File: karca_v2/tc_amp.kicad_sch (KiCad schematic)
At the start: 16 parts, among them U17 TLV9304xD, U22 AD8495

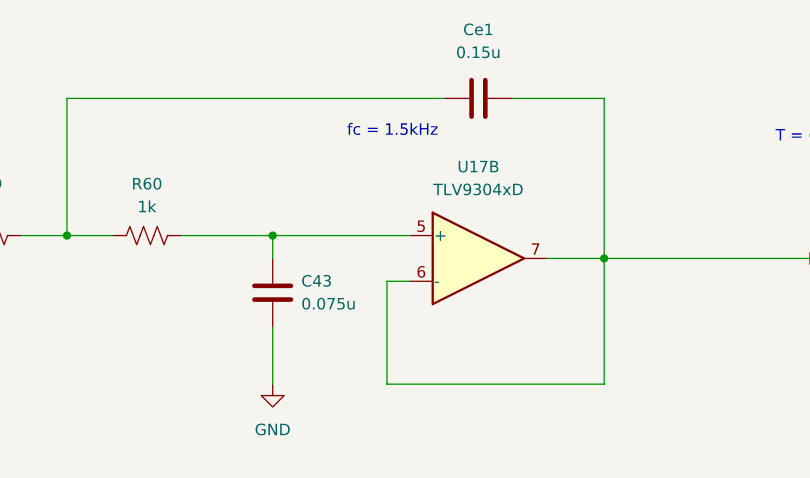
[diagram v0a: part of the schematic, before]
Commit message: changed capacitor values and sizes for production
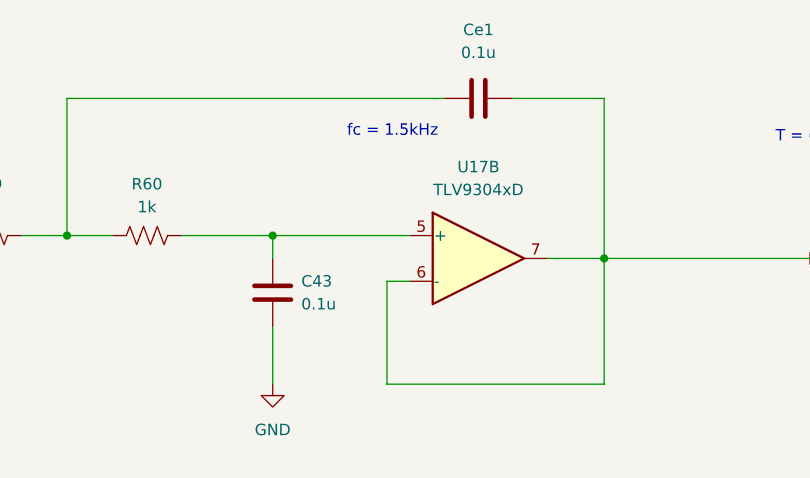
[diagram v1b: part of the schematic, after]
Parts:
- C43: value 0.075u -> 0.1u
- Ce1: value 0.15u -> 0.1u
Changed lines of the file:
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@@
       (effects (font (size 1.27 1.27)) (justify left))
     )
-    (property "Value" "0.075u" (at 196.85 62.23 0)
+    (property "Value" "0.1u" (at 196.85 62.23 0)
       (effects (font (size 1.27 1.27)) (justify left))
     )
@@
       (effects (font (size 1.27 1.27)))
     )
-    (property "Value" "0.15u" (at 216.535 34.29 90)
+    (property "Value" "0.1u" (at 216.535 34.29 90)
       (effects (font (size 1.27 1.27)))
     )

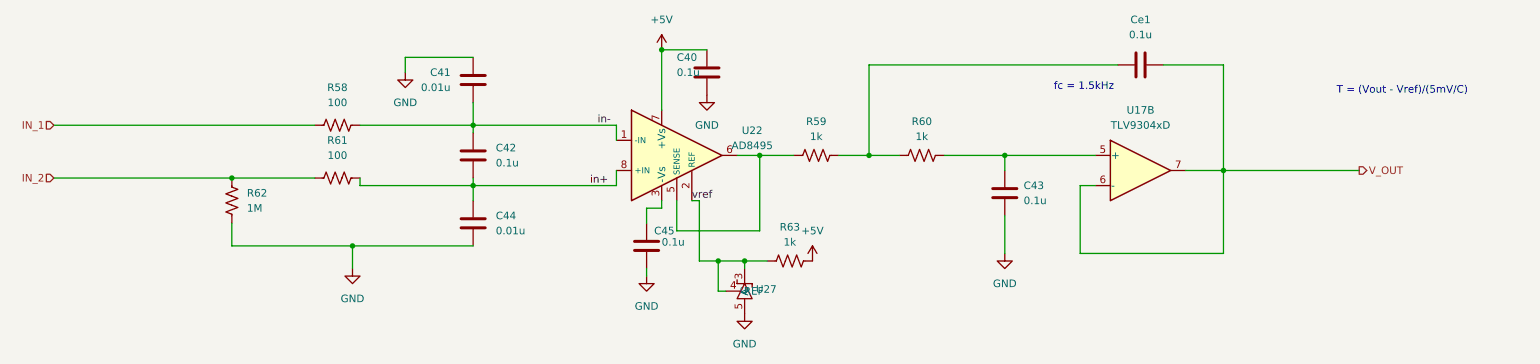
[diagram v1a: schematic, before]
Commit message: cleaned up documentation. Added production files and BOM. Marked Thermocouple components and THT components as DNP (excluded them from BOM too) to match version sent to JLCPCB for fabrication
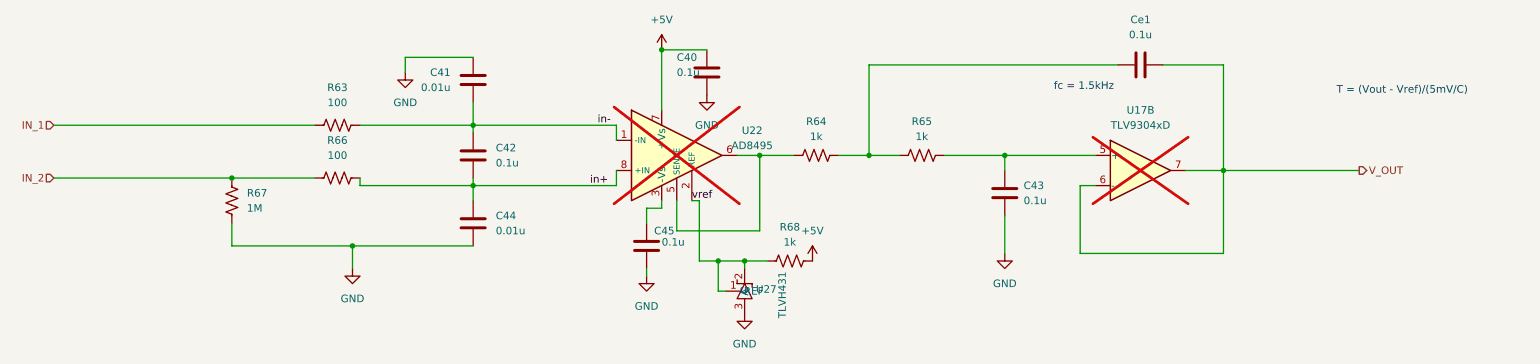
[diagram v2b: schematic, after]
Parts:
- C41, C44: footprint Capacitor_SMD:C_1206_3216Metric -> Capacitor_SMD:C_0402_1005Metric
- U17, U22: now not fitted; now left out of the parts list
- U27: value ~ -> TLVH431; footprint Package_TO_SOT_SMD:SOT-23-5 -> Package_TO_SOT_SMD:SOT-23
- renumbered R58 to R63, R59 to R64, R60 to R65, R61 to R66, R62 to R67, R63 to R68
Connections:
- net GND: now also U27.3 (A); no longer U27.5 (A)
- net vref: now also U27.1 (REF), U27.2 (C); no longer U27.3 (C), U27.4 (REF)
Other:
- company: (none) -> Rice Eclipse
- title: (none) -> kARCA 2.0 Engine Control System

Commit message: revisions for V2.1
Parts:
- removed C45: 0.1u, Capacitor_SMD:C_1206_3216Metric, symbol Device:C
- renumbered C40 to C52, C41 to C53, C42 to C54, C43 to C55, C44 to C56, Ce1 to Ce3, R63 to R75, R64 to R76, R65 to R77, R66 to R78, R67 to R79, R68 to R80, U22 to U26
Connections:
- net GND: now also U26.3 (-Vs)
- net V_OUT: now also U17.13 (-), U17.14; no longer U17.6 (-), U17.7
- net at C55.1, R77.2: now also U17.12 (+); no longer U17.5 (+)

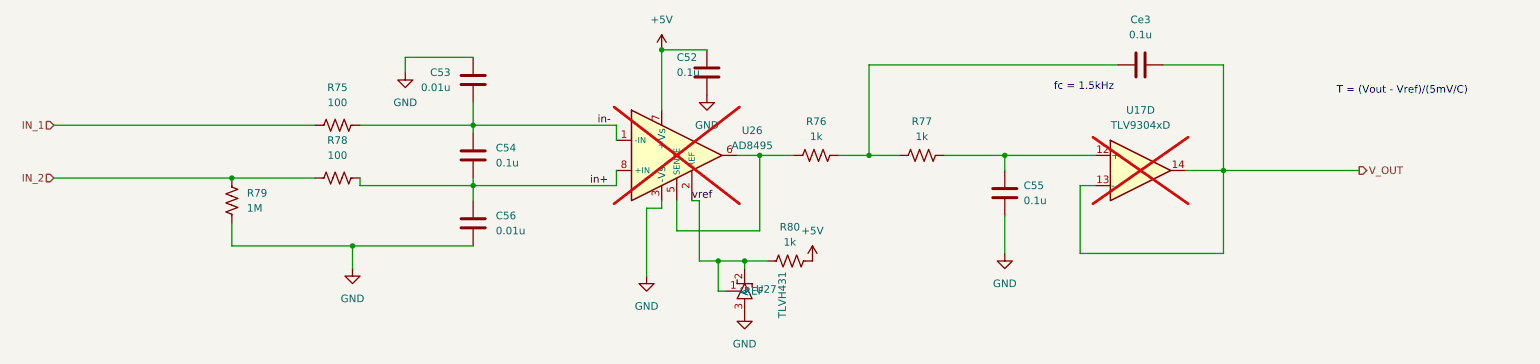
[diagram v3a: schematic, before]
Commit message: Replaced header with a smaller one, added silksreen labels, and removed secondary USB power source
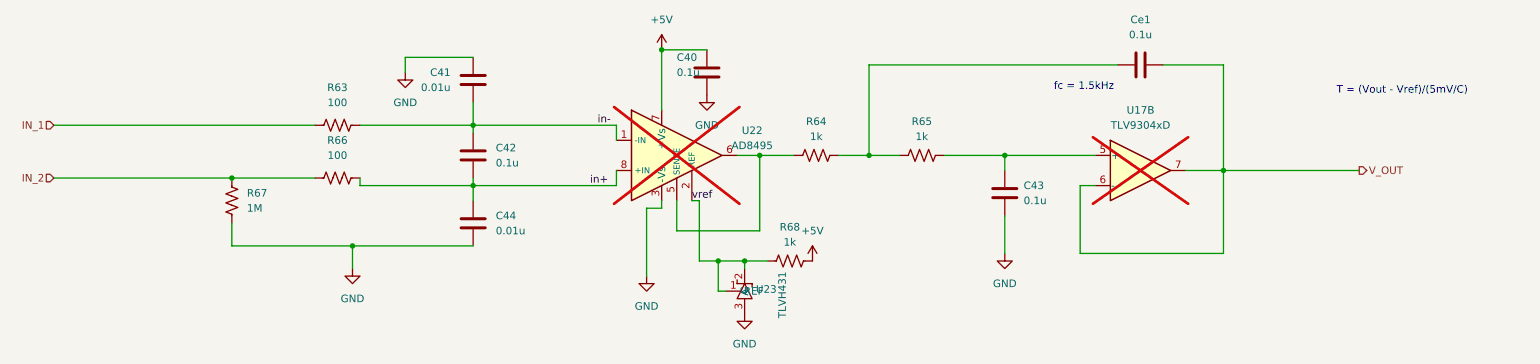
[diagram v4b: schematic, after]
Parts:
- renumbered C52 to C40, C53 to C41, C54 to C42, C55 to C43, C56 to C44, Ce3 to Ce1, R75 to R63, R76 to R64, R77 to R65, R78 to R66, R79 to R67, R80 to R68, U26 to U22, U27 to U23
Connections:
- net V_OUT: now also U17.6 (-), U17.7; no longer U17.13 (-), U17.14
- net at C43.1, R65.2: now also U17.5 (+); no longer U17.12 (+)
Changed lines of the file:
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@@
 (kicad_sch
-	(version 20231120)
+	(version 20250114)
 	(generator "eeschema")
-	(generator_version "8.0")
+	(generator_version "9.0")
 	(paper "A4")
 	(title_block
@@
 		(comment 2 "Engine Control System for the Static Engine Testing of Rice Eclipse's Hybrid Rocket Motors")
 	)
+	(text "T = (Vout - Vref)/(5mV/C)"
+		(exclude_from_sim no)
+		(at 249.555 44.45 0)
+		(effects
+			(font
+				(size 1.27 1.27)
+			)
+			(justify left bottom)
+		)
+	)
+	(text "fc = 1.5kHz\n"
+		(exclude_from_sim no)
+		(at 201.93 43.815 0)
+		(effects
+			(font
+				(size 1.27 1.27)
+			)
+			(justify left bottom)
+		)
+	)
 	(junction
 		(at 104.14 49.53)
@@
 			(width 0)
 			(type default)
-		)
-	)
-	(text "T = (Vout - Vref)/(5mV/C)"
-		(exclude_from_sim no)
-		(at 249.555 44.45 0)
-		(effects
-			(font
-				(size 1.27 1.27)
-			)
-			(justify left bottom)
-		)
-	)
-	(text "fc = 1.5kHz\n"
-		(exclude_from_sim no)
-		(at 201.93 43.815 0)
-		(effects
-			(font
-				(size 1.27 1.27)
-			)
-			(justify left bottom)
 		)
 	)
@@
 		(on_board yes)
 		(dnp no)
-		(property "Reference" "C52"
+		(property "Reference" "C40"
 			(at 138.43 38.1 0)
 			(effects
@@
 		(dnp no)
 		(fields_autoplaced yes)
-		(property "Reference" "C54"
+		(property "Reference" "C42"
 			(at 107.95 53.34 0)
 			(effects
@@
 		(dnp no)
 		(fields_autoplaced yes)
-		(property "Reference" "R76"
+		(property "Reference" "R64"
 			(at 161.925 48.895 90)
 			(effects
@@
 		(dnp no)
 		(fields_autoplaced yes)
-		(property "Reference" "#PWR0123"
+		(property "Reference" "#PWR0107"
 			(at 161.29 76.2 0)
 			(effects
@@
 		(dnp no)
 		(fields_autoplaced yes)
-		(property "Reference" "#PWR0125"
+		(property "Reference" "#PWR0109"
 			(at 133.35 81.28 0)
 			(effects
@@
 		(dnp no)
 		(fields_autoplaced yes)
-		(property "Reference" "#PWR0119"
+		(property "Reference" "#PWR0103"
 			(at 135.89 40.64 0)
 			(effects
@@
 		(dnp no)
 		(fields_autoplaced yes)
-		(property "Reference" "R75"
+		(property "Reference" "R63"
 			(at 81.28 43.18 90)
 			(effects
@@
 		(dnp no)
 		(fields_autoplaced yes)
-		(property "Reference" "#PWR0124"
+		(property "Reference" "#PWR0108"
 			(at 83.82 80.01 0)
 			(effects
@@
 		(dnp no)
 		(fields_autoplaced yes)
-		(property "Reference" "#PWR0126"
+		(property "Reference" "#PWR0110"
 			(at 149.86 87.63 0)
 			(effects
@@
 		(dnp no)
 		(fields_autoplaced yes)
-		(property "Reference" "#PWR0121"
+		(property "Reference" "#PWR0105"
 			(at 143.51 50.8 0)
 			(effects
@@
 		(on_board yes)
 		(dnp no)
-		(property "Reference" "U27"
+		(property "Reference" "U23"
 			(at 151.765 77.1525 90)
 			(effects
@@
 		(dnp no)
 		(fields_autoplaced yes)
-		(property "Reference" "#PWR0122"
+		(property "Reference" "#PWR0106"
 			(at 193.675 77.47 0)
 			(effects
@@
 		(lib_id "Amplifier_Operational:TLV9304xD")
 		(at 216.535 57.15 0)
-		(unit 4)
+		(unit 2)
 		(exclude_from_sim no)
 		(in_bom no)
@@
 		(on_board yes)
 		(dnp no)
-		(property "Reference" "C53"
+		(property "Reference" "C41"
 			(at 100.33 40.64 0)
 			(effects
@@
 		(dnp no)
 		(fields_autoplaced yes)
-		(property "Reference" "C55"
+		(property "Reference" "C43"
 			(at 196.85 59.69 0)
 			(effects
@@
 		(dnp no)
 		(fields_autoplaced yes)
-		(property "Reference" "Ce3"
+		(property "Reference" "Ce1"
 			(at 216.535 31.75 90)
 			(effects
@@
 		(dnp no)
 		(fields_autoplaced yes)
-		(property "Reference" "#PWR0120"
+		(property "Reference" "#PWR0104"
 			(at 92.71 46.99 0)
 			(effects
@@
 		(on_board yes)
 		(dnp yes)
-		(property "Reference" "U26"
+		(property "Reference" "U22"
 			(at 151.13 50.4191 0)
 			(effects
@@
 		(dnp no)
 		(fields_autoplaced yes)
-		(property "Reference" "R79"
+		(property "Reference" "R67"
 			(at 66.04 60.96 0)
 			(effects
@@
 		(dnp no)
 		(fields_autoplaced yes)
-		(property "Reference" "C56"
+		(property "Reference" "C44"
 			(at 107.95 64.77 0)
 			(effects
@@
 		(dnp no)
 		(fields_autoplaced yes)
-		(property "Reference" "R78"
+		(property "Reference" "R66"
 			(at 81.28 52.07 90)
 			(effects
@@
 		(dnp no)
 		(fields_autoplaced yes)
-		(property "Reference" "R80"
+		(property "Reference" "R68"
 			(at 157.48 66.675 90)
 			(effects
@@
 		(dnp no)
 		(fields_autoplaced yes)
-		(property "Reference" "R77"
+		(property "Reference" "R65"
 			(at 179.705 48.895 90)
 			(effects

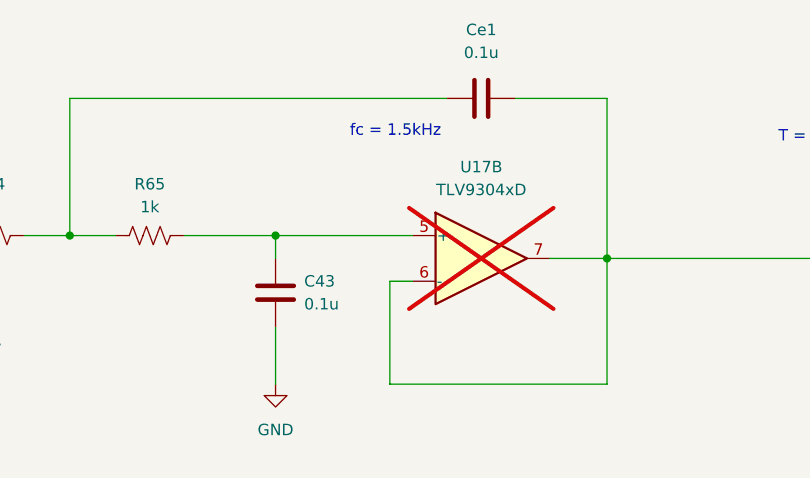
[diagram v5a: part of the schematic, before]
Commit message: finished schematic for v2.1
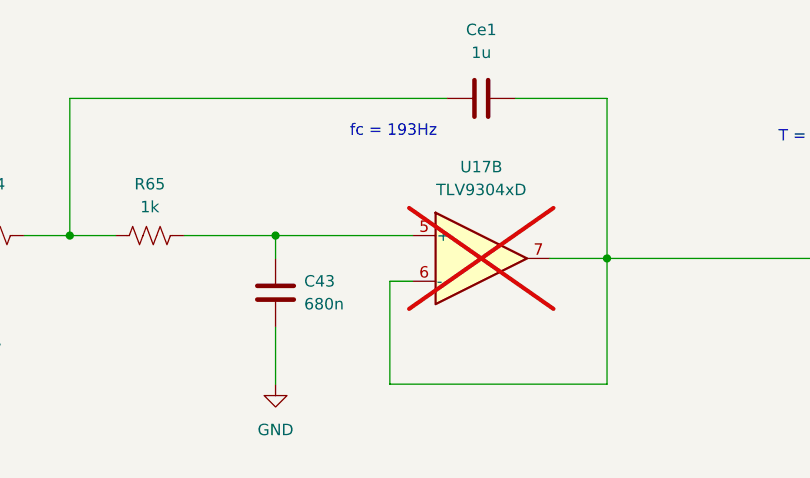
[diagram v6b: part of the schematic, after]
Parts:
- C43: value 0.1u -> 680n
- Ce1: value 0.1u -> 1u
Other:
- note added: "fc = 193Hz"
- note removed: "fc = 1.5kHz"
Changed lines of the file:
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@@
 		)
 	)
-	(text "fc = 1.5kHz\n"
+	(text "fc = 193Hz\n"
 		(exclude_from_sim no)
 		(at 201.93 43.815 0)
@@
 			)
 		)
-		(property "Value" "0.1u"
+		(property "Value" "680n"
 			(at 196.85 62.23 0)
 			(effects
@@
 			)
 		)
-		(property "Value" "0.1u"
+		(property "Value" "1u"
 			(at 216.535 34.29 90)
 			(effects

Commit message: swapped adcs
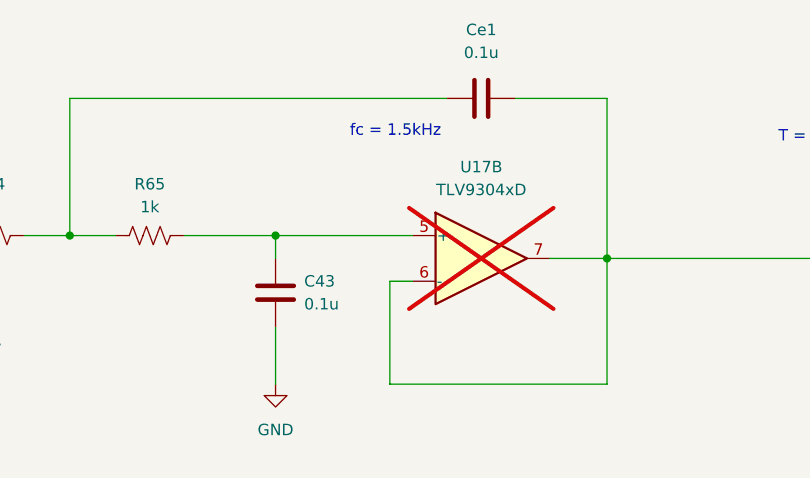
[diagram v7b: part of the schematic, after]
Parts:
- C43: value 680n -> 0.1u
- Ce1: value 1u -> 0.1u
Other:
- note added: "fc = 1.5kHz"
- note removed: "fc = 193Hz"
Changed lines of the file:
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@@
 	(title_block
 		(title "kARCA 2.0 Engine Control System")
-		(date "2026-03-23")
-		(rev "1.2")
+		(date "2024-12-16")
+		(rev "1.1")
 		(company "Rice Eclipse")
 		(comment 1 "Designed by Deepak Narayan")
@@
 		)
 	)
-	(text "fc = 193Hz\n"
+	(text "fc = 1.5kHz\n"
 		(exclude_from_sim no)
 		(at 201.93 43.815 0)
@@
 			)
 		)
-		(property "Value" "680n"
+		(property "Value" "0.1u"
 			(at 196.85 62.23 0)
 			(effects
@@
 			)
 		)
-		(property "Value" "1u"
+		(property "Value" "0.1u"
 			(at 216.535 34.29 90)
 			(effects

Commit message: All tests passed. Going to run DFM next
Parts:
- C43: value 0.1u -> 680n
- Ce1: value 0.1u -> 1u
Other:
- note added: "fc = 193Hz"
- note removed: "fc = 1.5kHz"
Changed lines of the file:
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@@
 	(title_block
 		(title "kARCA 2.0 Engine Control System")
-		(date "2024-12-16")
+		(date "2026-03-25")
 		(rev "1.1")
 		(company "Rice Eclipse")
@@
 		)
 	)
-	(text "fc = 1.5kHz\n"
+	(text "fc = 193Hz\n"
 		(exclude_from_sim no)
 		(at 201.93 43.815 0)
@@
 			)
 		)
-		(property "Value" "0.1u"
+		(property "Value" "680n"
 			(at 196.85 62.23 0)
 			(effects
@@
 			)
 		)
-		(property "Value" "0.1u"
+		(property "Value" "1u"
 			(at 216.535 34.29 90)
 			(effects
